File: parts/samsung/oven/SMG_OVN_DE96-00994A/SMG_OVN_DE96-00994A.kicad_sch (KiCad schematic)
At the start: 26 parts

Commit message: Minor design modifications
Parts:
- removed S1: SRRM1C7800, OpenSpare_footprints:SW_SRRM1C7800, symbol OpenSpare_symbols:SRRM1C7800
- added J1: Conn_01x04_Socket, Connector_JST:JST_XH_S4B-XH-A_1x04_P2.50mm_Horizontal, symbol Connector:Conn_01x04_Socket
- added RS1: 4P3T Rotary Switch, OpenSpare_footprints:SW_SRRM1C7800, symbol OpenSpare_symbols:RS240403A0X-HA1-000
- D1, D2, D3, D4, D5, D6, R14, R15, R16, R17, R18, R19: now not fitted; now left out of the parts list
- R1, R2, R3, R4, R5, R6: Manufacturer (none) -> YAGEO; Manufacturer1 (none) -> YAGEO; Manufacturer1Ref (none) -> RC0603FR-101KL; Manufacturer_alt (none) -> Yageo; RefManufacturer (none) -> RC0603FR-101KL; RefManufacturer_alt (none) -> RC0603FR-101KL; RefSupplier (none) -> 603-RC0603FR-101KL; Supplier (none) -> Mouser; Supplier1 (none) -> Mouser; Supplier1Ref (none) -> 603-RC0603FR-101KL
- R10, R7, R8, R9: Manufacturer (none) -> YAGEO; Manufacturer1 (none) -> YAGEO; Manufacturer1Ref (none) -> RC0603FR-102KL; RefManufacturer (none) -> RC0603FR-102KL; RefSupplier (none) -> 603-RC0603FR-102KL; Supplier (none) -> Mouser; Supplier1 (none) -> Mouser; Supplier1Ref (none) -> 603-RC0603FR-102KL
- R11, R12: Manufacturer (none) -> YAGEO; Manufacturer1 (none) -> YAGEO; Manufacturer1Ref (none) -> RC0603FR-134K7L; RefManufacturer (none) -> RC0603FR-134K7L; RefSupplier (none) -> 603-RC0603FR-134K7L; Supplier (none) -> Mouser; Supplier1 (none) -> Mouser; Supplier1Ref (none) -> 603-RC0603FR-134K7L
- R13: Manufacturer (none) -> YAGEO; Manufacturer1 (none) -> YAGEO; Manufacturer1Ref (none) -> RC0603JR-0710KL; RefManufacturer (none) -> RC0603JR-0710KL; RefSupplier (none) -> 603-RC0603JR-0710KL; Supplier (none) -> Mouser; Supplier1 (none) -> Mouser; Supplier1Ref (none) -> 603-RC0603JR-0710KL
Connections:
- net GND: now also J1.1 (Pin_1)
- net VDD: now also J1.4 (Pin_4)
- net LED_K: now reaches D1.1 (K), D2.1 (K), D3.1 (K), D4.1 (K), D5.1 (K), D6.1 (K)
- net LED_K: now also J1.2 (Pin_2)
- net at R4.1, R5.2: now also RS1.1
- net at R1.1, R2.2: now also RS1.10
- net at R2.1, R3.2: now also RS1.11
- net at R3.1, R4.2: now also RS1.12
- net OUT: now reaches R13.1
- net OUT: now also J1.3 (Pin_3), RS1.13, RS1.14, RS1.15, RS1.16
- net at R5.1, R6.2: now also RS1.2
- net at R6.1, R7.1: now also RS1.3
- net at R7.2, R8.1: now also RS1.4
- net at R8.2, R9.1: now also RS1.5
- net at R10.1, R9.2: now also RS1.6
- net at R10.2, R11.1: now also RS1.7
- net at R11.2, R12.1: now also RS1.8
- net at R12.2: now also RS1.9

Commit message: Update SMG_OVN_DE96-00994A design (rev 1)
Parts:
- removed J1: Conn_01x04_Socket, Connector_JST:JST_XH_S4B-XH-A_1x04_P2.50mm_Horizontal, symbol Connector:Conn_01x04_Socket
- added J1: Conn_01x04_Socket, OpenSpare_footprints:KON_C2502RD10403T0101PB, symbol OpenSpare_symbols:C2502RD10403T0101PB
- R1, R2, R3, R4, R5, R6: Manufacturer YAGEO -> (none); Manufacturer1 YAGEO -> (none); Manufacturer1Ref RC0603FR-101KL -> (none); Manufacturer1_Name (none) -> YAGEO; Manufacturer1_Part_Number (none) -> RC0603FR-101KL; Manufacturer_alt Yageo -> (none); RefManufacturer RC0603FR-101KL -> (none); RefManufacturer_alt RC0603FR-101KL -> (none); RefSupplier 603-RC0603FR-101KL -> (none); Supplier Mouser -> (none); Supplier1 Mouser -> (none); Supplier1Ref 603-RC0603FR-101KL -> (none); Supplier1_Name (none) -> Mouser; Supplier1_Part_Number (none) -> 603-RC0603FR-101KL
- R10, R7, R8, R9: Manufacturer YAGEO -> (none); Manufacturer1 YAGEO -> (none); Manufacturer1Ref RC0603FR-102KL -> (none); Manufacturer1_Name (none) -> YAGEO; Manufacturer1_Part_Number (none) -> RC0603FR-102KL; RefManufacturer RC0603FR-102KL -> (none); RefSupplier 603-RC0603FR-102KL -> (none); Supplier Mouser -> (none); Supplier1 Mouser -> (none); Supplier1Ref 603-RC0603FR-102KL -> (none); Supplier1_Name (none) -> Mouser; Supplier1_Part_Number (none) -> 603-RC0603FR-102KL
- R11, R12: Manufacturer YAGEO -> (none); Manufacturer1 YAGEO -> (none); Manufacturer1Ref RC0603FR-134K7L -> (none); Manufacturer1_Name (none) -> YAGEO; Manufacturer1_Part_Number (none) -> RC0603FR-134K7L; RefManufacturer RC0603FR-134K7L -> (none); RefSupplier 603-RC0603FR-134K7L -> (none); Supplier Mouser -> (none); Supplier1 Mouser -> (none); Supplier1Ref 603-RC0603FR-134K7L -> (none); Supplier1_Name (none) -> Mouser; Supplier1_Part_Number (none) -> 603-RC0603FR-134K7L
- R13: Manufacturer YAGEO -> (none); Manufacturer1 YAGEO -> (none); Manufacturer1Ref RC0603JR-0710KL -> (none); Manufacturer1_Name (none) -> YAGEO; Manufacturer1_Part_Number (none) -> RC0603JR-0710KL; RefManufacturer RC0603JR-0710KL -> (none); RefSupplier 603-RC0603JR-0710KL -> (none); Supplier Mouser -> (none); Supplier1 Mouser -> (none); Supplier1Ref 603-RC0603JR-0710KL -> (none); Supplier1_Name (none) -> Mouser; Supplier1_Part_Number (none) -> 603-RC0603JR-0710KL
- R14: value 10k -> (none)
- R15, R16, R17, R18, R19: value 10k -> ~
- RS1: footprint OpenSpare_footprints:SW_SRRM1C7800 -> OpenSpare_footprints:SW_RS240403A0X-HA1-000; Manufacturer1 SOUNDWELL ELECTRONIC -> (none); Manufacturer1Ref RS240403A0X-HA1-000 -> (none); Manufacturer1_Name (none) -> SOUNDWELL ELECTRONIC; Manufacturer1_Part_Number (none) -> RS240403A0X-HA1-000; Manufacturer2 ALPS -> (none); Manufacturer2Ref SRRM1C7800 -> (none); Manufacturer2_Name (none) -> ALPS; Manufacturer2_Part_Number (none) -> SRRM1C7800
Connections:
- net GND: now also J1.1
- net LED_K: now also J1.2
- net OUT: now also J1.3
- net VDD: now also J1.4

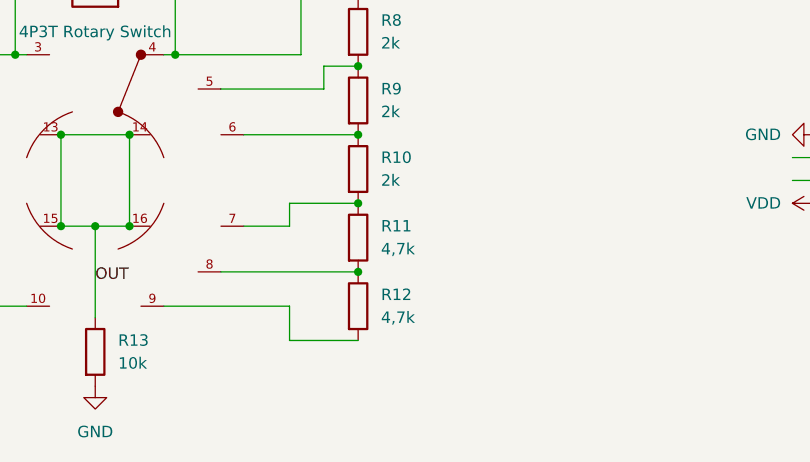
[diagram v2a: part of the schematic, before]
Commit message: Generate output for JLCPCB format
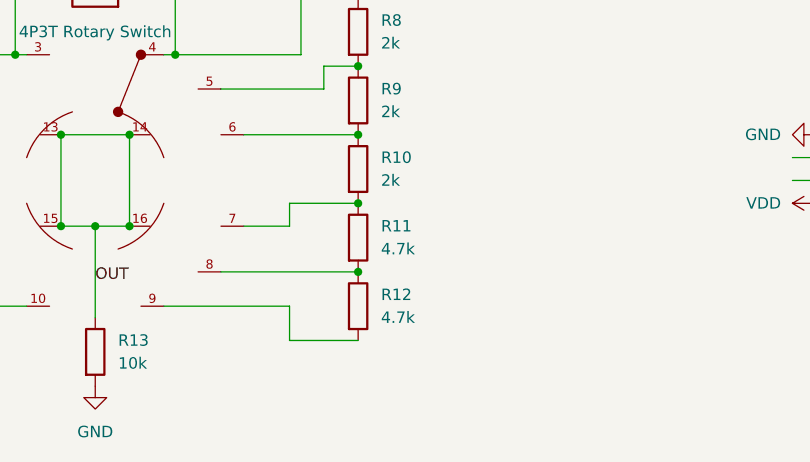
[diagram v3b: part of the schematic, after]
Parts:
- J1: LCSC Part # (none) -> C9900221323
- R1, R2, R3, R4, R5, R6: LCSC Part # (none) -> C1512170
- R10, R7, R8, R9: LCSC Part # (none) -> C4103683
- R11, R12: value 4,7k -> 4.7k; LCSC Part # (none) -> C4269355
- R13: LCSC Part # (none) -> C4004838; Manufacturer1_Part_Number RC0603JR-0710KL -> RC0603FR-1010KL; Supplier1_Part_Number 603-RC0603JR-0710KL -> 603-RC0603FR-1010KL
- R14: value (none) -> ~
- RS1: LCSC Part # (none) -> C9900221322
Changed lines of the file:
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@@
 			)
 		)
-		(property "Value" ""
+		(property "Value" "~"
 			(at 46.99 83.8199 0)
 			(effects
@@
 			)
 		)
+		(property "LCSC Part #" "C4103683"
+			(at 181.61 72.39 0)
+			(effects
+				(font
+					(size 1.27 1.27)
+				)
+				(hide yes)
+			)
+		)
 		(pin "1"
 		)
@@
 			)
 		)
-		(property "Description" "Thick Film Resistors - SMD General Purpose Chip Resistor 0603, 10kOhms, 5%, 1/10W"
+		(property "Description" "Thick Film Resistors - SMD General Purpose Chip Resistor 0603, 10kOhms, 1%, 1/10W"
 			(at 152.4 107.95 0)
 			(effects
@@
 			)
 		)
-		(property "Supplier1_Part_Number" "603-RC0603JR-0710KL"
+		(property "Supplier1_Part_Number" " 603-RC0603FR-1010KL"
 			(at 152.4 107.95 0)
 			(effects
@@
 			)
 		)
-		(property "Manufacturer1_Part_Number" "RC0603JR-0710KL"
+		(property "Manufacturer1_Part_Number" "RC0603FR-1010KL"
 			(at 152.4 107.95 0)
 			(effects
@@
 			)
 		)
+		(property "LCSC Part #" "C4004838"
+			(at 152.4 107.95 0)
+			(effects
+				(font
+					(size 1.27 1.27)
+				)
+				(hide yes)
+			)
+		)
 		(pin "1"
 		)
@@
 			)
 		)
+		(property "LCSC Part #" "C4103683"
+			(at 181.61 80.01 0)
+			(effects
+				(font
+					(size 1.27 1.27)
+				)
+				(hide yes)
+			)
+		)
 		(pin "1"
 		)
@@
 			)
 		)
+		(property "LCSC Part #" "C1512170"
+			(at 120.65 80.01 0)
+			(effects
+				(font
+					(size 1.27 1.27)
+				)
+				(hide yes)
+			)
+		)
 		(pin "1"
 		)
@@
 			)
 		)
+		(property "LCSC Part #" "C1512170"
+			(at 120.65 102.87 0)
+			(effects
+				(font
+					(size 1.27 1.27)
+				)
+				(hide yes)
+			)
+		)
 		(pin "1"
 		)
@@
 			)
 		)
+		(property "LCSC Part #" "C1512170"
+			(at 120.65 87.63 0)
+			(effects
+				(font
+					(size 1.27 1.27)
+				)
+				(hide yes)
+			)
+		)
 		(pin "1"
 		)
@@
 			)
 		)
+		(property "LCSC Part #" "C1512170"
+			(at 120.65 95.25 0)
+			(effects
+				(font
+					(size 1.27 1.27)
+				)
+				(hide yes)
+			)
+		)
 		(pin "1"
 		)
@@
 			)
 		)
+		(property "LCSC Part #" "C4103683"
+			(at 152.4 68.58 90)
+			(effects
+				(font
+					(size 1.27 1.27)
+				)
+				(hide yes)
+			)
+		)
 		(pin "1"
 		)
@@
 			)
 		)
+		(property "LCSC Part #" "C4103683"
+			(at 181.61 87.63 0)
+			(effects
+				(font
+					(size 1.27 1.27)
+				)
+				(hide yes)
+			)
+		)
 		(pin "1"
 		)
@@
 			)
 		)
-		(property "Value" "4,7k"
+		(property "Value" "4.7k"
 			(at 184.15 104.1399 0)
 			(effects
@@
 			)
 		)
+		(property "LCSC Part #" "C4269355"
+			(at 181.61 102.87 0)
+			(effects
+				(font
+					(size 1.27 1.27)
+				)
+				(hide yes)
+			)
+		)
 		(pin "1"
 		)
@@
 			)
 		)
+		(property "LCSC Part #" "C1512170"
+			(at 113.03 102.87 0)
+			(effects
+				(font
+					(size 1.27 1.27)
+				)
+				(hide yes)
+			)
+		)
 		(pin "1"
 		)
@@
 			)
 		)
-		(property "Value" "4,7k"
+		(property "Value" "4.7k"
 			(at 184.15 96.5199 0)
 			(effects
@@
 			)
 		)
+		(property "LCSC Part #" "C4269355"
+			(at 181.61 95.25 0)
+			(effects
+				(font
+					(size 1.27 1.27)
+				)
+				(hide yes)
+			)
+		)
 		(pin "1"
 		)
@@
 			)
 		)
+		(property "LCSC Part #" "C9900221322"
+			(at 219.71 88.9 0)
+			(effects
+				(font
+					(size 1.27 1.27)
+				)
+				(hide yes)
+			)
+		)
 		(pin "14"
 		)
@@
 			)
 		)
+		(property "LCSC Part #" "C1512170"
+			(at 120.65 72.39 0)
+			(effects
+				(font
+					(size 1.27 1.27)
+				)
+				(hide yes)
+			)
+		)
 		(pin "1"
 		)
@@
 			(at 240.03 87.63 0)
 			(effects
+				(font
+					(size 1.27 1.27)
+				)
+				(hide yes)
+			)
+		)
+		(property "LCSC Part #" "C9900221323"
+			(at 240.03 87.63 0)
+			(effects

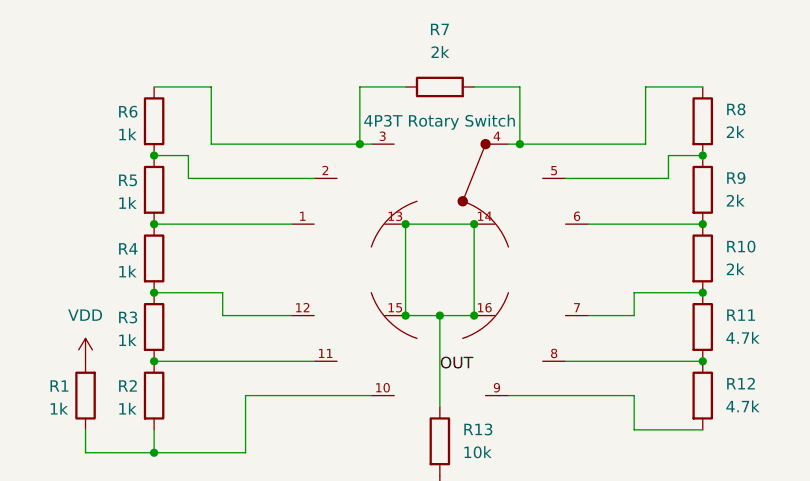
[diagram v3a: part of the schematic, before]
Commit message: Increase SMG_OVN_DE96-00994A 's revision to 1.1/Tested by fixing component reference for the rotary switch RS1
- Replace ref RS240403A0X-HA1-000 by the -020 version that has correct output connection specifications
- Set ALPS SRRM1C7800 as prefered part number for RS1 (the one tested)
- Improve schematics and pcb to better indicate connection requirements
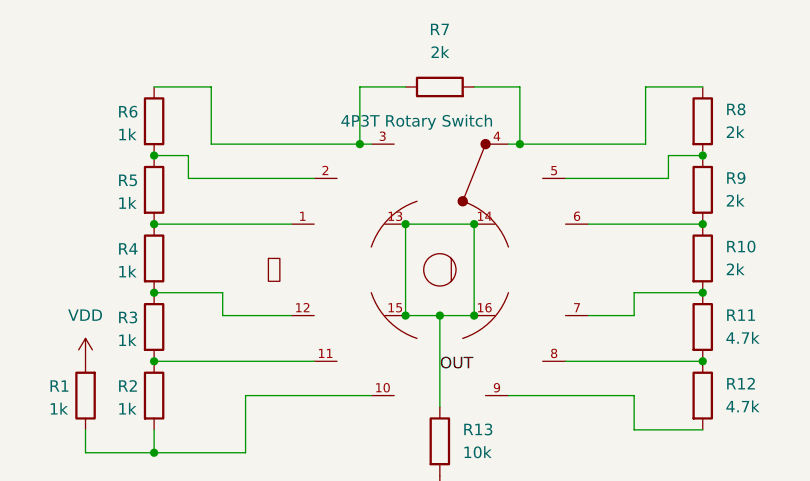
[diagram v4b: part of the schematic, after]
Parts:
- removed RS1: 4P3T Rotary Switch, OpenSpare_footprints:SW_RS240403A0X-HA1-000, symbol OpenSpare_symbols:RS240403A0X-HA1-000
- added RS1: 4P3T Rotary Switch, OpenSpare_footprints:SW_RS240403A0X-HA1-020, symbol OpenSpare_symbols:RS240403A0X-HA1-020
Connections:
- net OUT: now also RS1.13, RS1.14, RS1.15, RS1.16
- net at R7.2, R8.1: now also RS1.4
- net at R8.2, R9.1: now also RS1.5
- net at R10.1, R9.2: now also RS1.6
- net at R5.1, R6.2: now also RS1.2
- net at R4.1, R5.2: now also RS1.1
- net at R2.1, R3.2: now also RS1.11
- net at R1.1, R2.2: now also RS1.10
- net at R3.1, R4.2: now also RS1.12
- net at R6.1, R7.1: now also RS1.3
- net at R10.2, R11.1: now also RS1.7
- net at R11.2, R12.1: now also RS1.8
- net at R12.2: now also RS1.9
